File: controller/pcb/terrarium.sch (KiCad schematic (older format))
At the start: 56 parts, among them Q1 S8050, Q2 S8050, Q3 S8050, SW1 RESET, SW2 BOOT, SW3 RESET RTC, U1 ESP32-WROOM-32, U2 DS3231M, U3 LM1117-3.3

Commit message: minor updates, bjt to sot-23
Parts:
- Q3: footprint Package_TO_SOT_THT:TO-92_Inline -> Package_TO_SOT_SMD:SOT-23; symbol Transistor_BJT:S8050 -> Device:Q_NPN_BEC
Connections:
- net GND: now also Q3.2 (E); no longer Q3.1 (E)
- net at R7.2: now also Q3.1 (B); no longer Q3.2 (B)
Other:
- moved on the sheet: LED3, R7
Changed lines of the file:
@@
 	1    0    0    -1
 $EndComp
-Text GLabel 5950 5050 0    50   Input ~ 0
+Text GLabel 5850 5400 0    50   Input ~ 0
 G25
 $Comp
@@
 Text GLabel 9000 2950 0    50   Input ~ 0
 220N
-$Comp
-L Transistor_BJT:S8050 Q3
-U 1 1 61BD2EC2
-P 6950 5350
-F 0 "Q3" H 7150 5350 50  0000 L CNN
-F 1 "S8050" H 6800 5200 50  0000 L CNN
-F 2 "Package_TO_SOT_THT:TO-92_Inline" H 7150 5275 50  0001 L CIN
-F 3 "https://www.onsemi.com/pub/Collateral/2N3903-D.PDF" H 6950 5350 50  0001 L CNN
-	1    6950 5350
-	1    0    0    -1
-$EndComp
 Text GLabel 5900 1900 0    50   Input ~ 0
 G5
@@
 L power:GND #PWR01
 U 1 1 61BD2EC9
-P 6600 5700
-F 0 "#PWR01" H 6600 5450 50  0001 C CNN
-F 1 "GND" V 6605 5572 50  0000 R CNN
-F 2 "" H 6600 5700 50  0001 C CNN
-F 3 "" H 6600 5700 50  0001 C CNN
-	1    6600 5700
-	0    1    1    0
+P 7000 5750
+F 0 "#PWR01" H 7000 5500 50  0001 C CNN
+F 1 "GND" V 7005 5622 50  0000 R CNN
+F 2 "" H 7000 5750 50  0001 C CNN
+F 3 "" H 7000 5750 50  0001 C CNN
+	1    7000 5750
+	1    0    0    -1
 $EndComp
 $Comp
 L Device:R_Small R7
 U 1 1 61BD2ECF
-P 6600 5050
-F 0 "R7" V 6700 5050 50  0000 C CNN
-F 1 "150ohm" V 6500 5050 50  0000 C CNN
-F 2 "Resistor_SMD:R_1206_3216Metric" H 6600 5050 50  0001 C CNN
-F 3 "~" H 6600 5050 50  0001 C CNN
-	1    6600 5050
+P 6500 5400
+F 0 "R7" V 6600 5400 50  0000 C CNN
+F 1 "150ohm" V 6400 5400 50  0000 C CNN
+F 2 "Resistor_SMD:R_1206_3216Metric" H 6500 5400 50  0001 C CNN
+F 3 "~" H 6500 5400 50  0001 C CNN
+	1    6500 5400
 	0    -1   -1   0
 $EndComp
@@
 L Device:LED LED3
 U 1 1 61BD2ED5
-P 6250 5050
-F 0 "LED3" H 6350 4950 50  0000 R CNN
-F 1 "ACTIVE" H 6350 5150 50  0000 R CNN
-F 2 "LED_SMD:LED_1206_3216Metric" H 6250 5050 50  0001 C CNN
-F 3 "~" H 6250 5050 50  0001 C CNN
-	1    6250 5050
+P 6150 5400
+F 0 "LED3" H 6250 5300 50  0000 R CNN
+F 1 "ACTIVE" H 6250 5500 50  0000 R CNN
+F 2 "LED_SMD:LED_1206_3216Metric" H 6150 5400 50  0001 C CNN
+F 3 "~" H 6150 5400 50  0001 C CNN
+	1    6150 5400
 	-1   0    0    1
 $EndComp
@@
 	7350 5150 7350 5050
 Wire Wire Line
-	5950 5050 6100 5050
-Wire Wire Line
-	6400 5050 6500 5050
-Wire Wire Line
-	6700 5050 6750 5050
-Wire Wire Line
-	6750 5050 6750 5350
+	5850 5400 6000 5400
+Wire Wire Line
+	6300 5400 6400 5400
 Wire Wire Line
 	7850 5050 7350 5050
 Connection ~ 7350 5050
-Wire Wire Line
-	7050 5550 7050 5700
 $Comp
 L Diode:1N47xxA D3
@@
 	0    -1   -1   0
 $EndComp
-Wire Wire Line
-	7150 5150 7050 5150
-Wire Wire Line
-	6600 5700 7050 5700
 $Comp
 L Relay:SANYOU_SRD_Form_C RE3
@@
 Wire Wire Line
 	3250 7850 3250 7800
+$Comp
+L Device:Q_NPN_BEC Q3
+U 1 1 61BD2EC2
+P 6900 5400
+F 0 "Q3" H 7100 5400 50  0000 L CNN
+F 1 "S8050" H 6750 5250 50  0000 L CNN
+F 2 "Package_TO_SOT_SMD:SOT-23" H 7100 5325 50  0001 L CIN
+F 3 "https://www.onsemi.com/pub/Collateral/2N3903-D.PDF" H 6900 5400 50  0001 L CNN
+	1    6900 5400
+	1    0    0    -1
+$EndComp
+Wire Wire Line
+	6600 5400 6700 5400
+Wire Wire Line
+	7150 5150 7000 5150
+Wire Wire Line
+	7000 5150 7000 5200
+Wire Wire Line
+	7000 5750 7000 5600
 $EndSCHEMATC

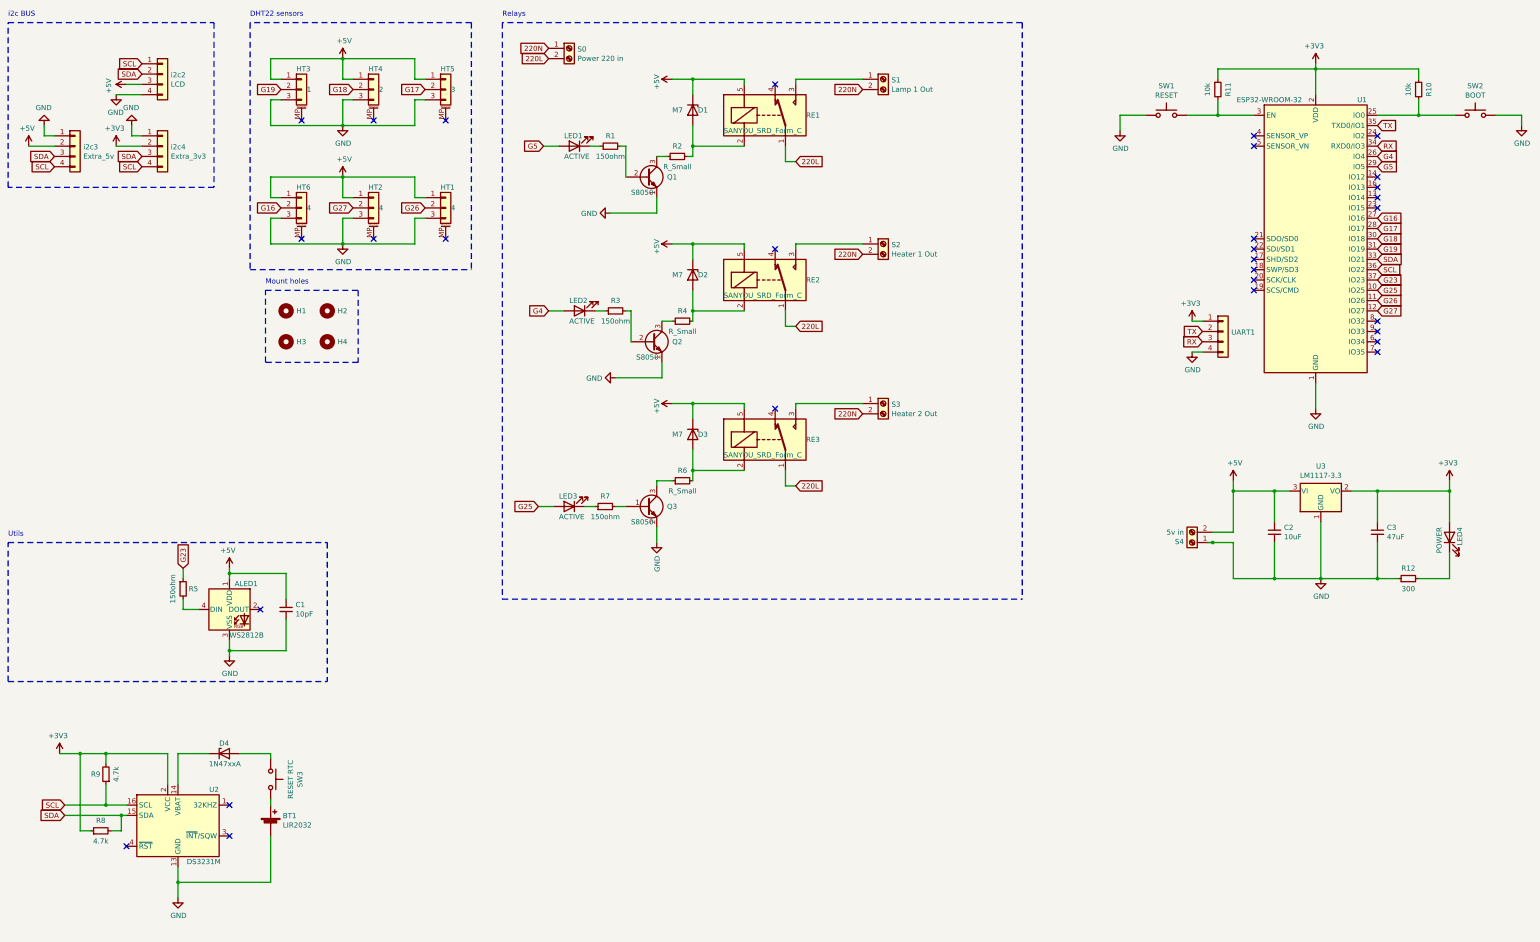
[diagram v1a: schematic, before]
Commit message: rtc charge, refactoring
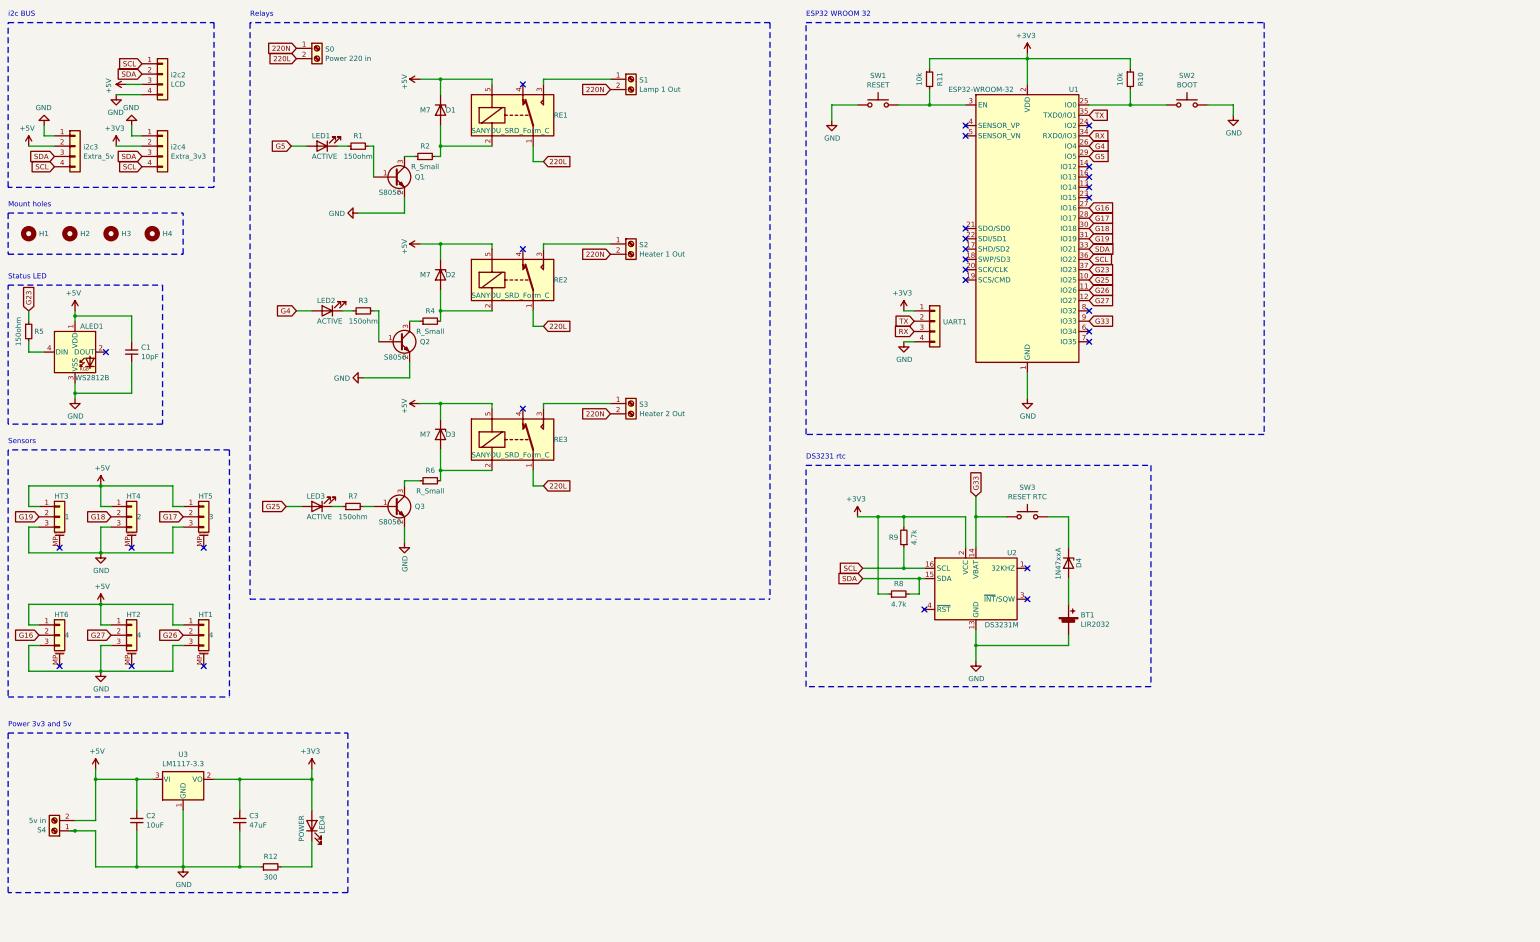
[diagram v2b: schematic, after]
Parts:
- removed Q1, Q2: S8050, Package_TO_SOT_THT:TO-92_Inline, symbol Transistor_BJT:S8050
- added Q1, Q2: S8050, Package_TO_SOT_SMD:SOT-23, symbol Device:Q_NPN_BEC
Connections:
- net GND: now also Q1.2 (E), Q2.2 (E)
- net at R4.1: now also Q2.3 (C)
- net at R2.1: now also Q1.3 (C)
- net at R1.2: now also Q1.1 (B)
- net at D4.1 (K): now also SW3.2; no longer U2.14 (VBAT)
- net G33: now reaches U1.9 (IO33)
- net G33: now also SW3.1, U2.14 (VBAT)
- net at R3.2: now also Q2.1 (B)
- net at BT1.1 (+): now also D4.2 (A); no longer SW3.2
- no-connect marks 30 -> 29
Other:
- note added: "DS3231 rtc"
- note added: "ESP32 WROOM 32"
- note added: "Power 3v3 and 5v"
- note added: "Sensors"
- note added: "Status LED"
- note removed: "DHT22 sensors"
- note removed: "Utils"
- moved on the sheet: ALED1, BT1, C1, C2, C3, D1, D2, D3, D4, H1, H2, H3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

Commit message: minor changes
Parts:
- D1, D2, D3: footprint Diode_SMD:D_2114_3652Metric -> Diode_SMD:D_2010_5025Metric
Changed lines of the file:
@@
 F 0 "D1" V 4900 1600 50  0000 L CNN
 F 1 "M7" V 4900 1350 50  0000 L CNN
-F 2 "Diode_SMD:D_2114_3652Metric" H 4900 1375 50  0001 C CNN
+F 2 "Diode_SMD:D_2010_5025Metric" H 4900 1375 50  0001 C CNN
 F 3 "https://www.vishay.com/docs/85816/1n4728a.pdf" H 4900 1550 50  0001 C CNN
 	1    4900 1550
@@
 F 0 "D2" V 4900 3200 50  0000 L CNN
 F 1 "M7" V 4900 2950 50  0000 L CNN
-F 2 "Diode_SMD:D_2114_3652Metric" H 4900 2975 50  0001 C CNN
+F 2 "Diode_SMD:D_2010_5025Metric" H 4900 2975 50  0001 C CNN
 F 3 "https://www.vishay.com/docs/85816/1n4728a.pdf" H 4900 3150 50  0001 C CNN
 	1    4900 3150
@@
 F 0 "D3" V 4900 4750 50  0000 L CNN
 F 1 "M7" V 4900 4500 50  0000 L CNN
-F 2 "Diode_SMD:D_2114_3652Metric" H 4900 4525 50  0001 C CNN
+F 2 "Diode_SMD:D_2010_5025Metric" H 4900 4525 50  0001 C CNN
 F 3 "https://www.vishay.com/docs/85816/1n4728a.pdf" H 4900 4700 50  0001 C CNN
 	1    4900 4700

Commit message: diode for battery
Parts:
- D4: footprint Diode_SMD:D_1206_3216Metric -> Diode_SMD:D_2010_5025Metric
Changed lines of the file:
@@
 F 0 "D4" H 10950 6050 50  0000 L CNN
 F 1 "1N47xxA" H 10850 5850 50  0000 L CNN
-F 2 "Diode_SMD:D_1206_3216Metric" H 11000 5775 50  0001 C CNN
+F 2 "Diode_SMD:D_2010_5025Metric" H 11000 5775 50  0001 C CNN
 F 3 "https://www.vishay.com/docs/85816/1n4728a.pdf" H 11000 5950 50  0001 C CNN
 	1    11000 5950

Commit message: fix bugs in UART
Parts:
- removed R10: 10k, Resistor_SMD:R_1206_3216Metric, symbol Device:R_Small
- removed SW2: BOOT, Button_Switch_SMD:SW_DIP_SPSTx01_Slide_6.7x4.1mm_W6.73mm_P2.54mm_LowProfile_JPin, symbol Switch:SW_Push
- added RESET_j1: data, Connector_PinHeader_2.54mm:PinHeader_1x02_P2.54mm_Vertical, symbol Connector_Generic:Conn_01x02
- added TP1, TP2: TestPoint, TestPoint:TestPoint_Pad_1.5x1.5mm, symbol Connector:TestPoint
- UART1: footprint Connector_PinHeader_2.54mm:PinHeader_1x04_P2.54mm_Vertical -> Connector_PinHeader_2.54mm:PinHeader_1x06_P2.54mm_Vertical; symbol Connector_Generic:Conn_01x04 -> Connector_Generic:Conn_01x06
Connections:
- net +3V3: now also UART1.2 (Pin_2); no longer UART1.1 (Pin_1)
- net GND: now also UART1.1 (Pin_1); no longer UART1.4 (Pin_4)
- net RX: now also UART1.4 (Pin_4); no longer UART1.3 (Pin_3)
- net TX: now also UART1.3 (Pin_3); no longer UART1.2 (Pin_2)
- net IO0: now reaches U1.25 (IO0)
- net IO0: now also UART1.5 (Pin_5)
- net at R11.2, SW1.2: now also RESET_j1.1 (Pin_1), TP2.1; no longer U1.3 (EN)
- new net EN: RESET_j1.2 (Pin_2), TP1.1, U1.3 (EN), UART1.6 (Pin_6)
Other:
- moved on the sheet: R11, SW1, U1

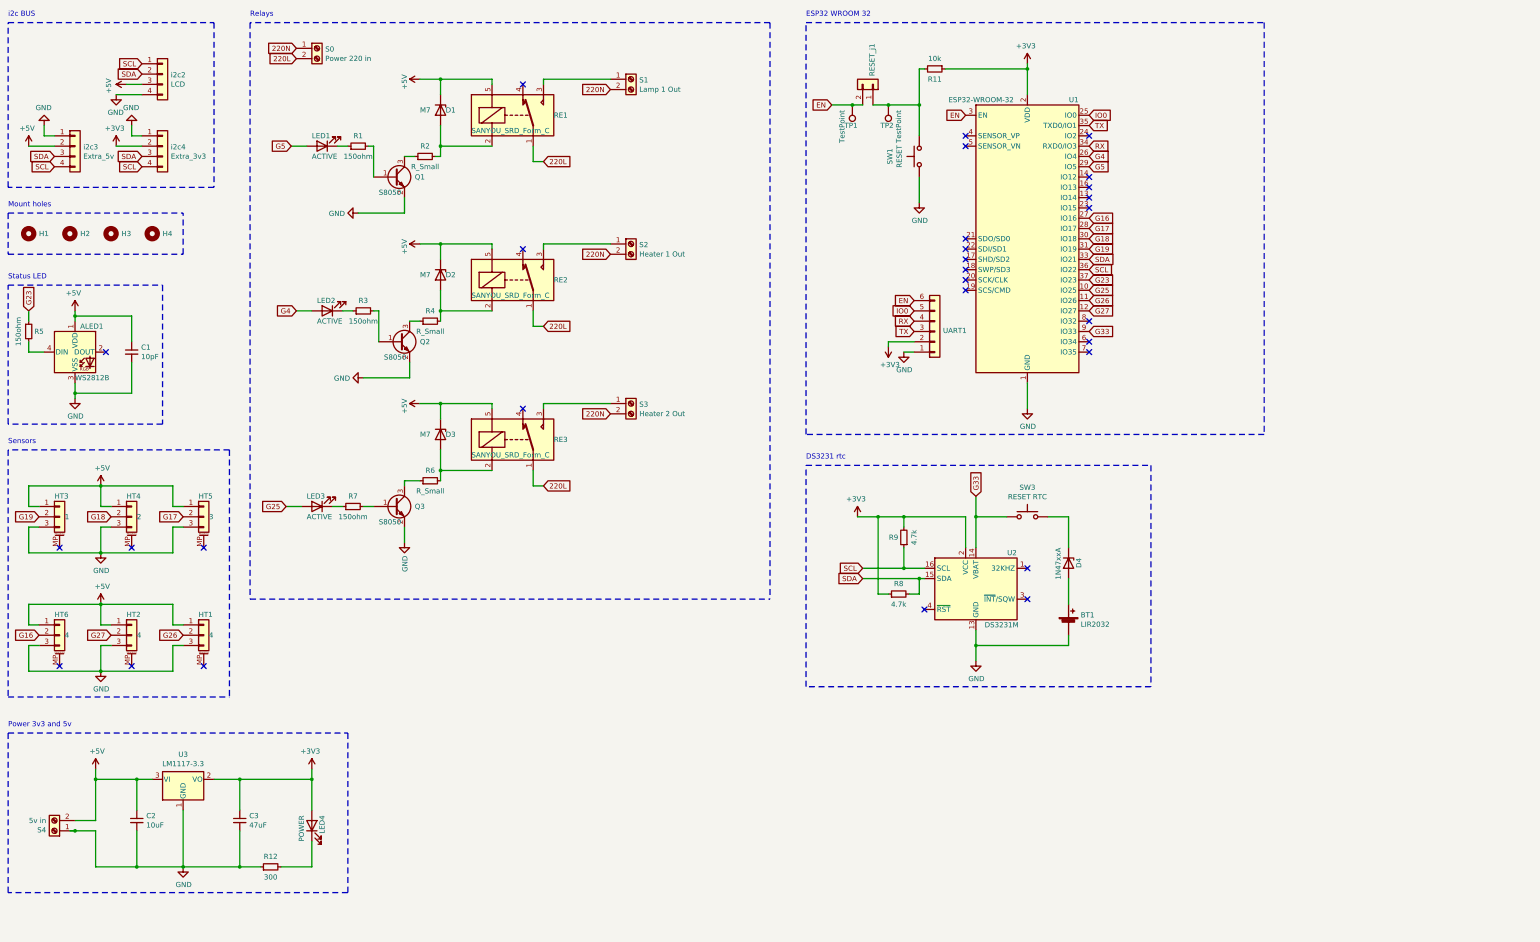
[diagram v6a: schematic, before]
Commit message: add transistor for sensors
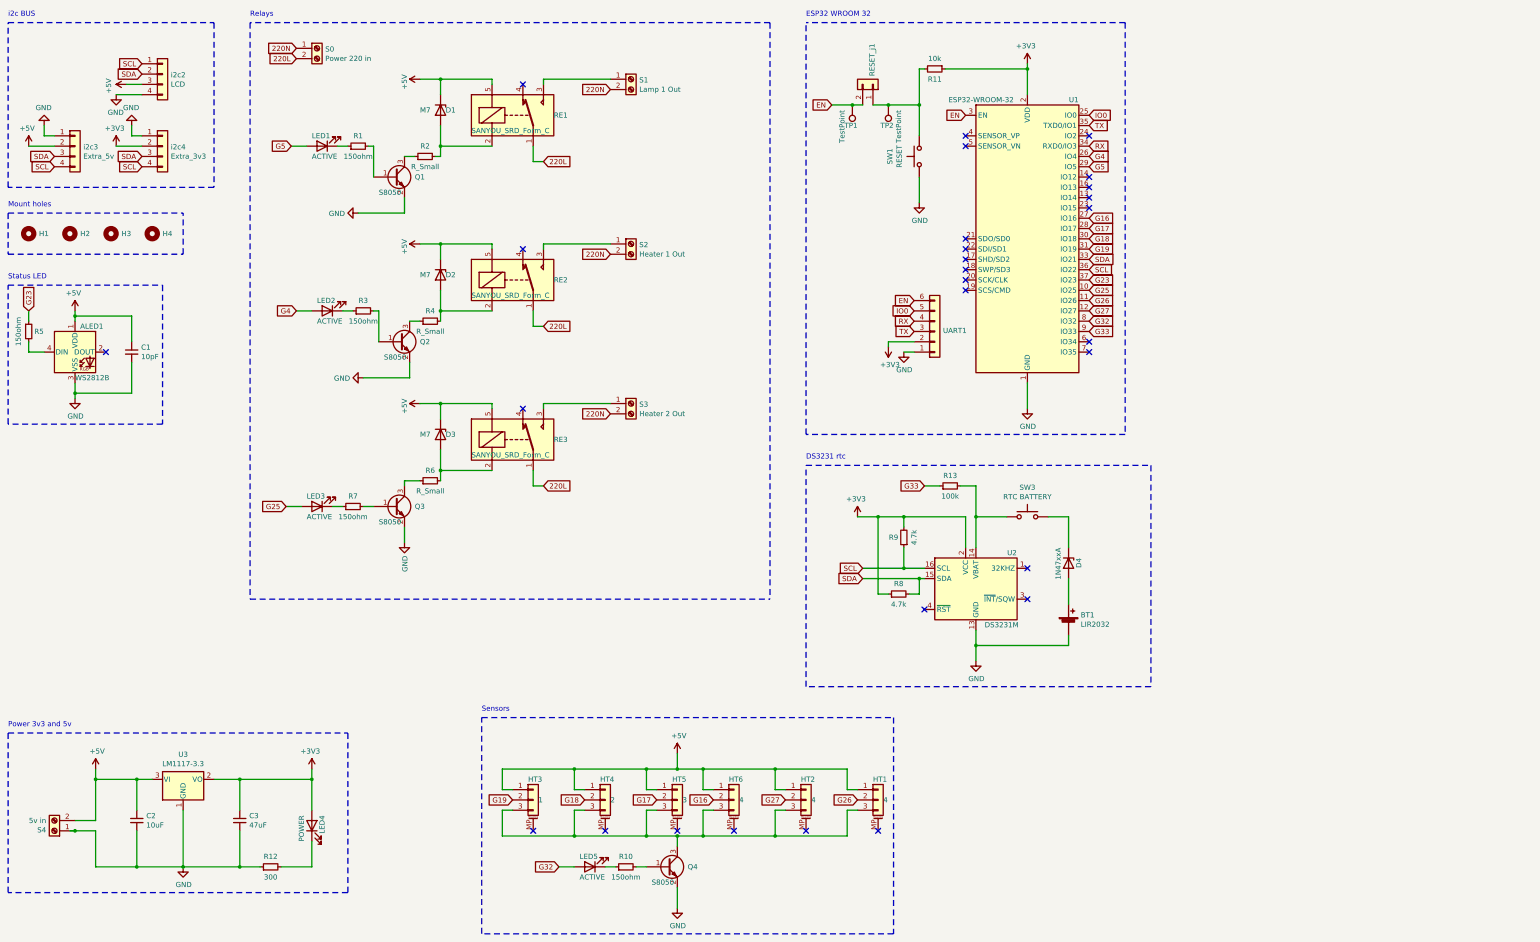
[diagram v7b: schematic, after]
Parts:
- added LED5: ACTIVE, LED_SMD:LED_1206_3216Metric, symbol Device:LED
- added Q4: S8050, Package_TO_SOT_SMD:SOT-23, symbol Device:Q_NPN_BEC
- added R10: 150ohm, Resistor_SMD:R_1206_3216Metric, symbol Device:R_Small
- added R13: 100k, Resistor_SMD:R_1206_3216Metric, symbol Device:R_Small
- SW3: value RESET RTC -> RTC BATTERY
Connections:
- net G33: now also R13.1; no longer SW3.1, U2.14 (VBAT)
- net GND: now also Q4.2 (E); no longer HT1.3 (Pin_3), HT2.3 (Pin_3), HT3.3 (Pin_3), HT4.3 (Pin_3), HT5.3 (Pin_3), HT6.3 (Pin_3)
- net G32: now reaches U1.8 (IO32)
- net G32: now also LED5.2 (A)
- new net: HT1.3 (Pin_3), HT2.3 (Pin_3), HT3.3 (Pin_3), HT4.3 (Pin_3), HT5.3 (Pin_3), HT6.3 (Pin_3), Q4.3 (C)
- new net: R13.2, SW3.1, U2.14 (VBAT)
- new net: LED5.1 (K), R10.1
- new net: Q4.1 (B), R10.2
- no-connect marks 29 -> 28
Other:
- moved on the sheet: HT1, HT2, HT3, HT4, HT5, HT6
